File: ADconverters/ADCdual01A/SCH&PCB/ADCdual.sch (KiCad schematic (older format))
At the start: 6 parts

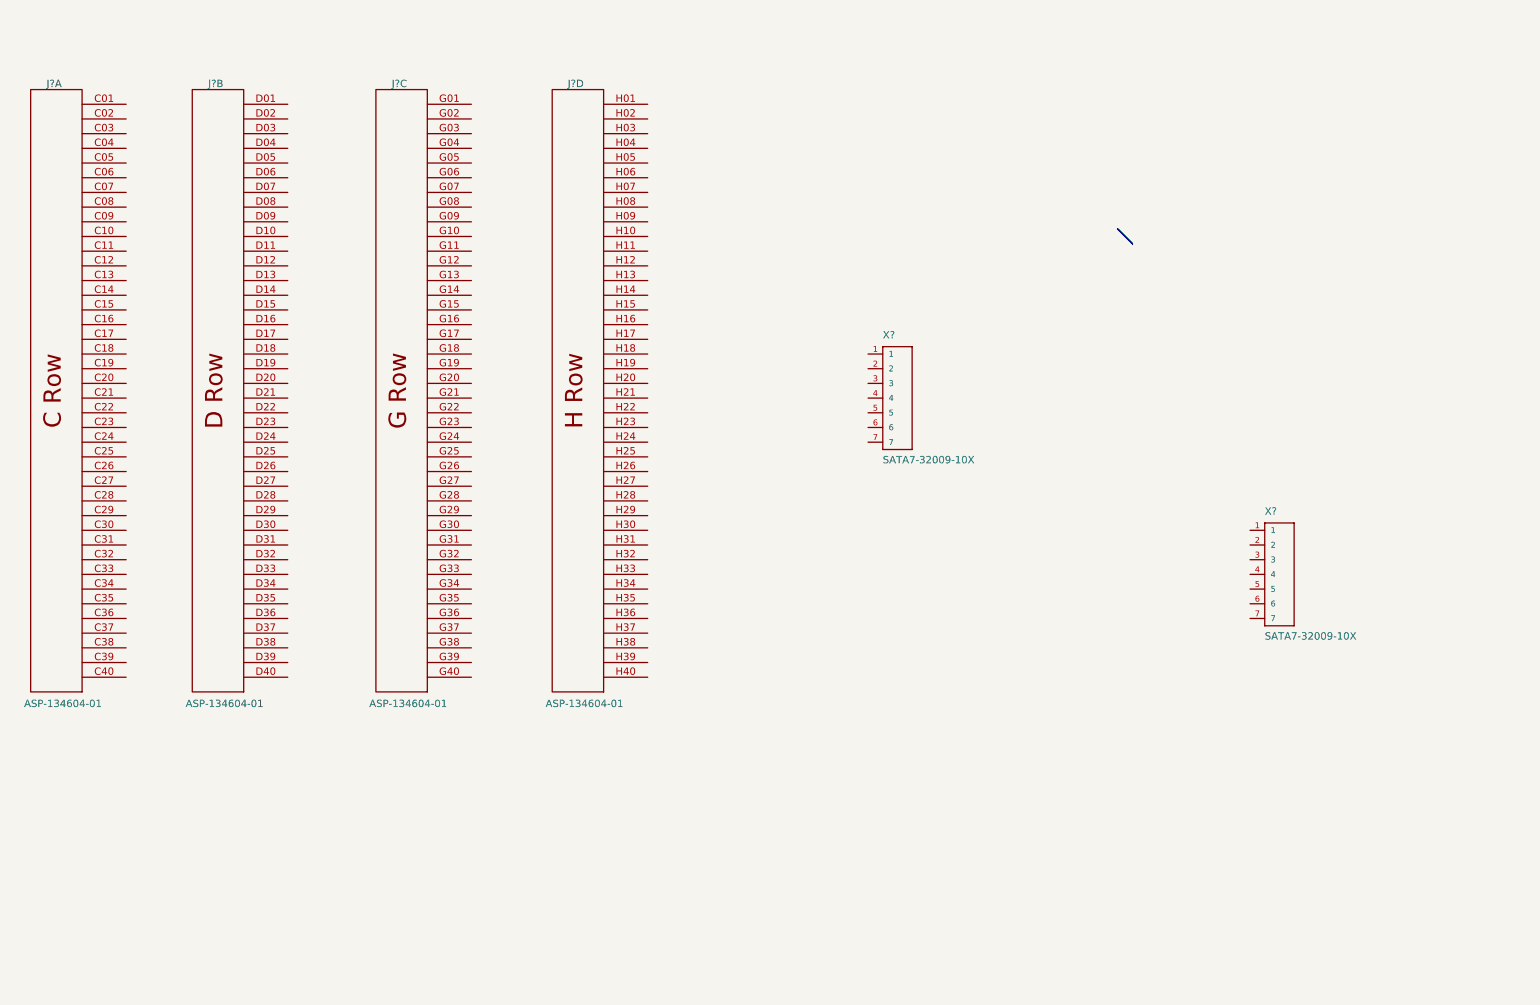
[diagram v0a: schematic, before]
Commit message: dokoncovani navrhu plosneho spoje pro FMC redukci (pridany koty). Zacatek navrhu modulu pro ADC.
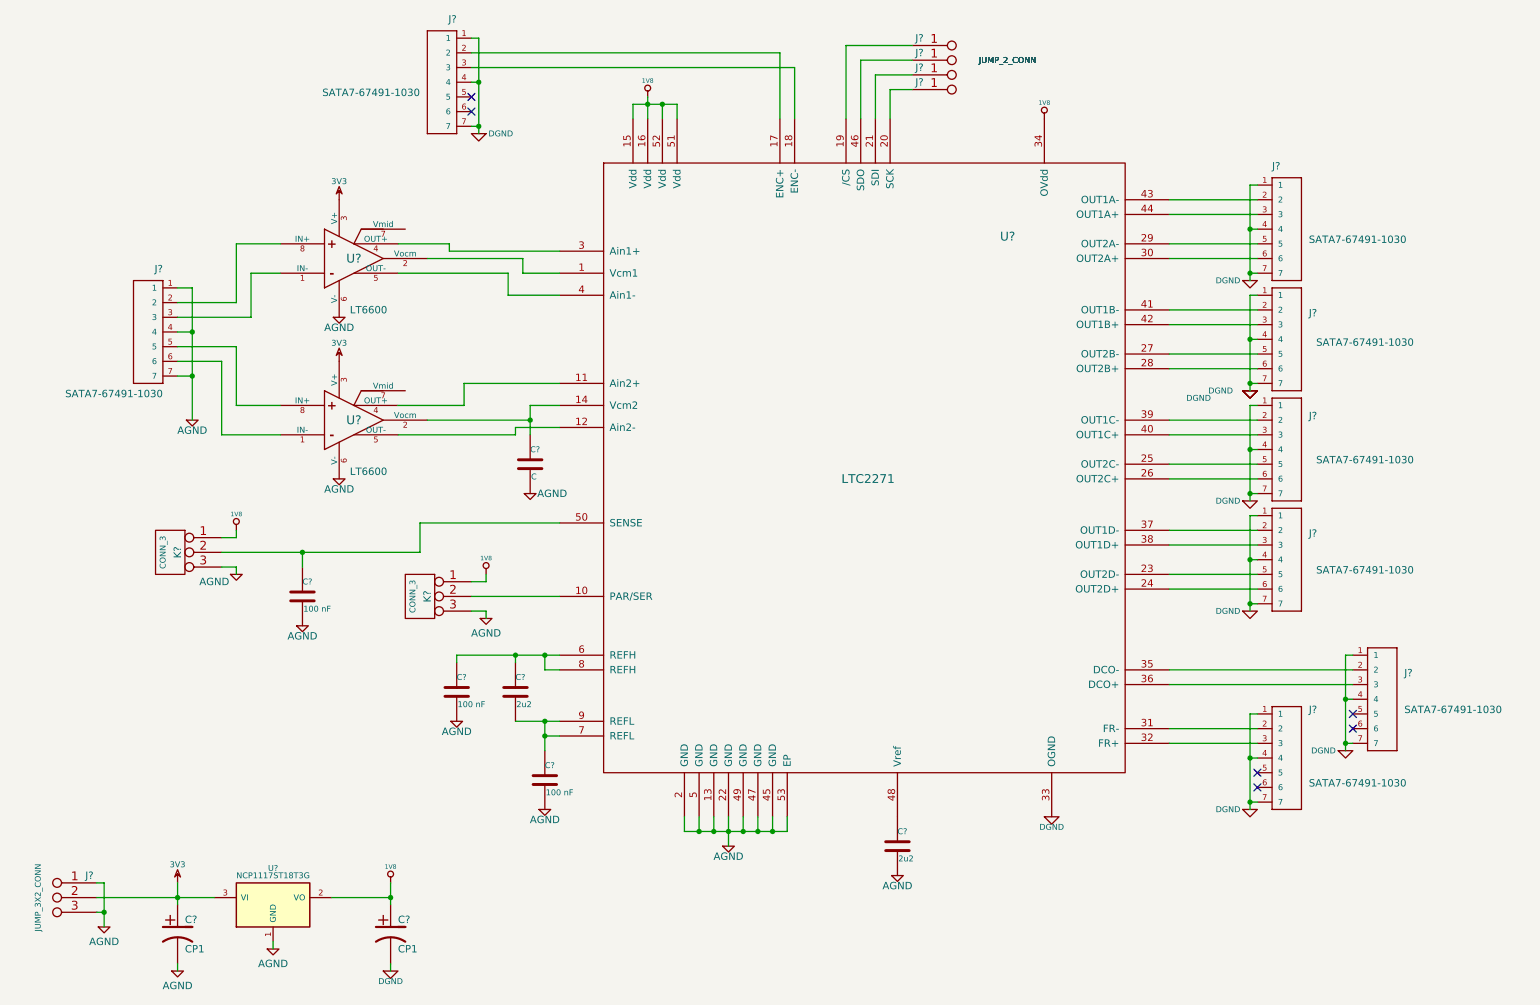
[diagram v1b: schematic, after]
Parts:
- removed J? (x4): ASP-134604-01_(FMC), FMC, symbol ASP-134604-01_(FMC)
- removed X? (x2): SATA7-32009-10X, con-cypressindustries-CCATA_32009_10X, symbol SATA7-32009-10X
- added C?: C, symbol C
- added C? (x2): CP1, symbol CP1
- added C? (x2): 2u2, symbol C
- added C? (x3): 100 nF, symbol C
- added J? (x8): SATA7-67491-1030, MOLEX_67491-1030, symbol SATA7-67491-1030
- added J?: JUMP_3X2_CONN, symbol JUMP_3X2_CONN
- added J? (x4): JUMP_2_CONN, symbol JUMP_2_CONN
- added K? (x2): CONN_3, symbol CONN_3
- added U? (x2): LT6600, symbol LT6600
- added U?: LTC2271, symbol LTC2271
- added U?: NCP1117ST18T3G, symbol NCP1117ST18T3G
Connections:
- new net: J?.2, U?.8 (IN+)
- new net: J?.3, U?.1 (IN-)
- new net: J?.5, U?.8 (IN+)
- new net: J?.6, U?.1 (IN-)
- new net: J?.2, U?.43 (OUT1A-)
- new net: J?.3, U?.44 (OUT1A+)
- new net: J?.5, U?.29 (OUT2A-)
- new net: J?.6, U?.30 (OUT2A+)
- new net: U?.1 (Vcm1), U?.2 (Vocm)
- new net: U?.3 (Ain1+), U?.4 (OUT+)
- new net: U?.4 (Ain1-), U?.5 (OUT-)
- new net: C?.1, U?.14 (Vcm2), U?.2 (Vocm)
- new net: U?.11 (Ain2+), U?.4 (OUT+)
- new net: U?.12 (Ain2-), U?.5 (OUT-)
- new net: J?.2, U?.41 (OUT1B-)
- new net: J?.3, U?.42 (OUT1B+)
- new net: J?.5, U?.27 (OUT2B-)
- new net: J?.6, U?.28 (OUT2B+)
- new net: J?.2, U?.39 (OUT1C-)
- new net: J?.3, U?.40 (OUT1C+)
- new net: J?.5, U?.25 (OUT2C-)
- new net: J?.6, U?.26 (OUT2C+)
- new net: J?.2, U?.37 (OUT1D-)
- new net: J?.3, U?.38 (OUT1D+)
- new net: J?.5, U?.23 (OUT2D-)
- new net: J?.6, U?.24 (OUT2D+)
- new net: K?.2 (PM), U?.10 (PAR/SER)
- new net: J?.2, U?.17 (ENC+)
- new net: J?.3, U?.18 (ENC-)
- new net: J?.1, J?.2 (1), U?.19 (/CS)
- new net: J?.1, J?.2 (1), U?.20 (SCK)
- new net: J?.1, J?.2 (1), U?.21 (SDI)
- new net: J?.2, U?.31 (FR-)
- new net: J?.3, U?.32 (FR+)
- new net: J?.2, U?.35 (DCO-)
- new net: J?.3, U?.36 (DCO+)
- new net: J?.1, J?.2 (1), U?.46 (SDO)
- new net: C?.1, U?.48 (Vref)
- new net: C?.1, K?.2 (PM), U?.50 (SENSE)
- new net: C?.1, C?.1, U?.6 (REFH), U?.8 (REFH)
- new net: C?.1, C?.2, U?.7 (REFL), U?.9 (REFL)
- new net +1.8V: C?.1, K?.1 (P1), K?.1 (P1), U?.15 (Vdd), U?.16 (Vdd), U?.2 (VO), U?.34 (OVdd), U?.51 (Vdd), U?.52 (Vdd)
- new net 3V3: C?.1, J?.2 (1), J?.5, U?.3 (V+), U?.3 (V+), U?.3 (VI)
- new net AGND: C?.2, C?.2, C?.2, C?.2, C?.2, C?.2, J?.1, J?.1, J?.3, J?.4, J?.4, J?.6, J?.7, K?.3 (P3), K?.3 (P3), U?.1 (GND), U?.13 (GND), U?.2 (GND), U?.22 (GND), U?.45 (GND), U?.47 (GND), U?.49 (GND), U?.5 (GND), U?.53 (EP), U?.6 (V-), U?.6 (V-)
- new net DGND: C?.2, J?.1, J?.1, J?.1, J?.1, J?.1, J?.1, J?.1, J?.4, J?.4, J?.4, J?.4, J?.4, J?.4, J?.4, J?.7, J?.7, J?.7, J?.7, J?.7, J?.7, J?.7, U?.33 (OGND)
- no-connect marks 0 -> 6
